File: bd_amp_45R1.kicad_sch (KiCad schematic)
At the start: 53 parts, among them Q2101 2SC3357, Q2102 2SC3357, T2101 XFMR_RF_BIFILAR, T2102 XFMR_RF_BIFILAR, U2101 AS169-73, U2102 AS169-73

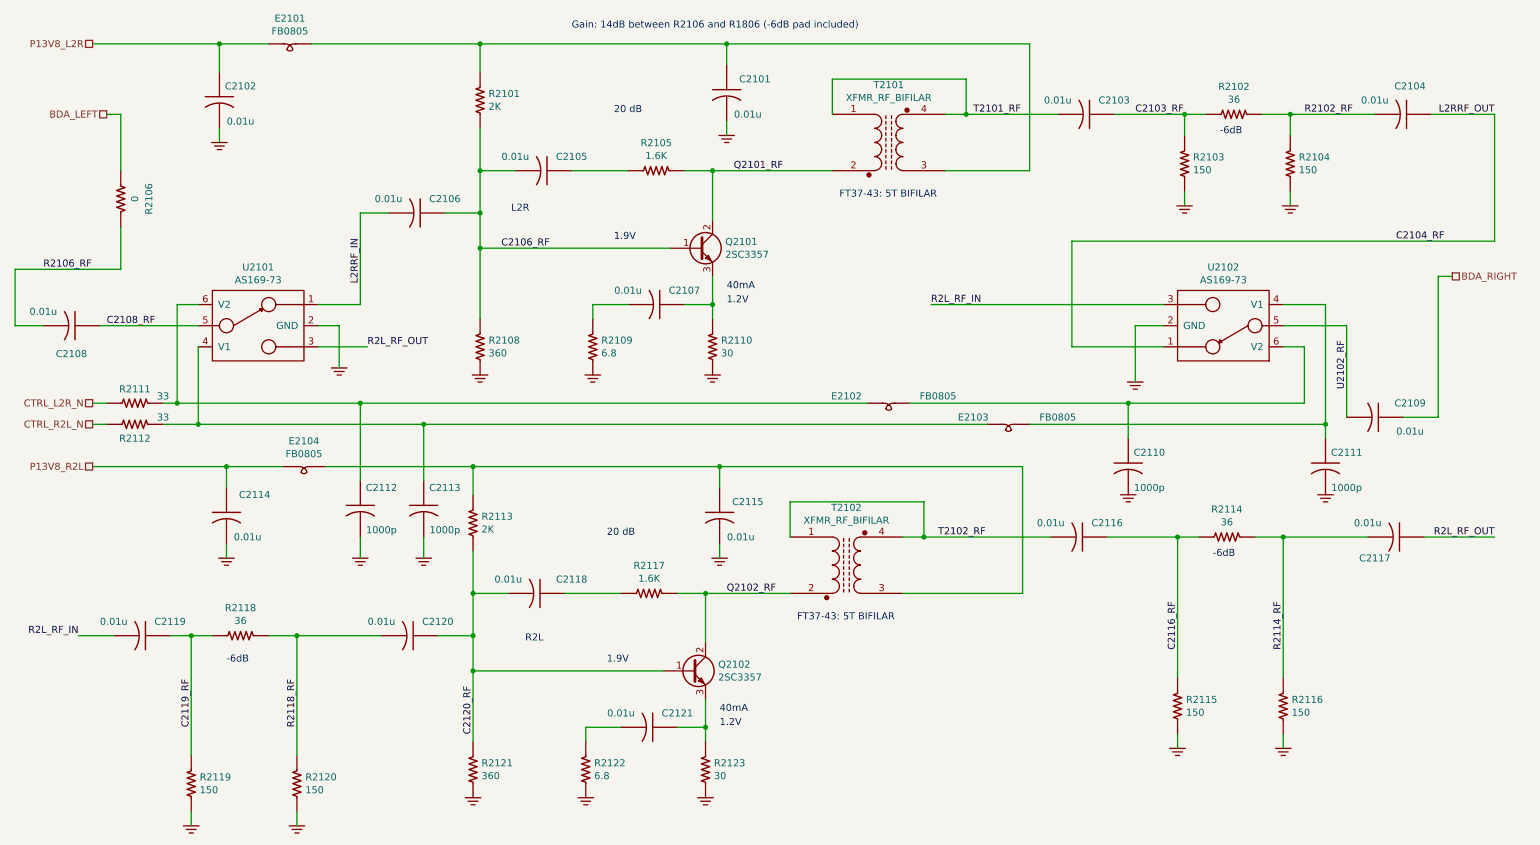
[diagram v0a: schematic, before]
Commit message: Update pcb database to version 6
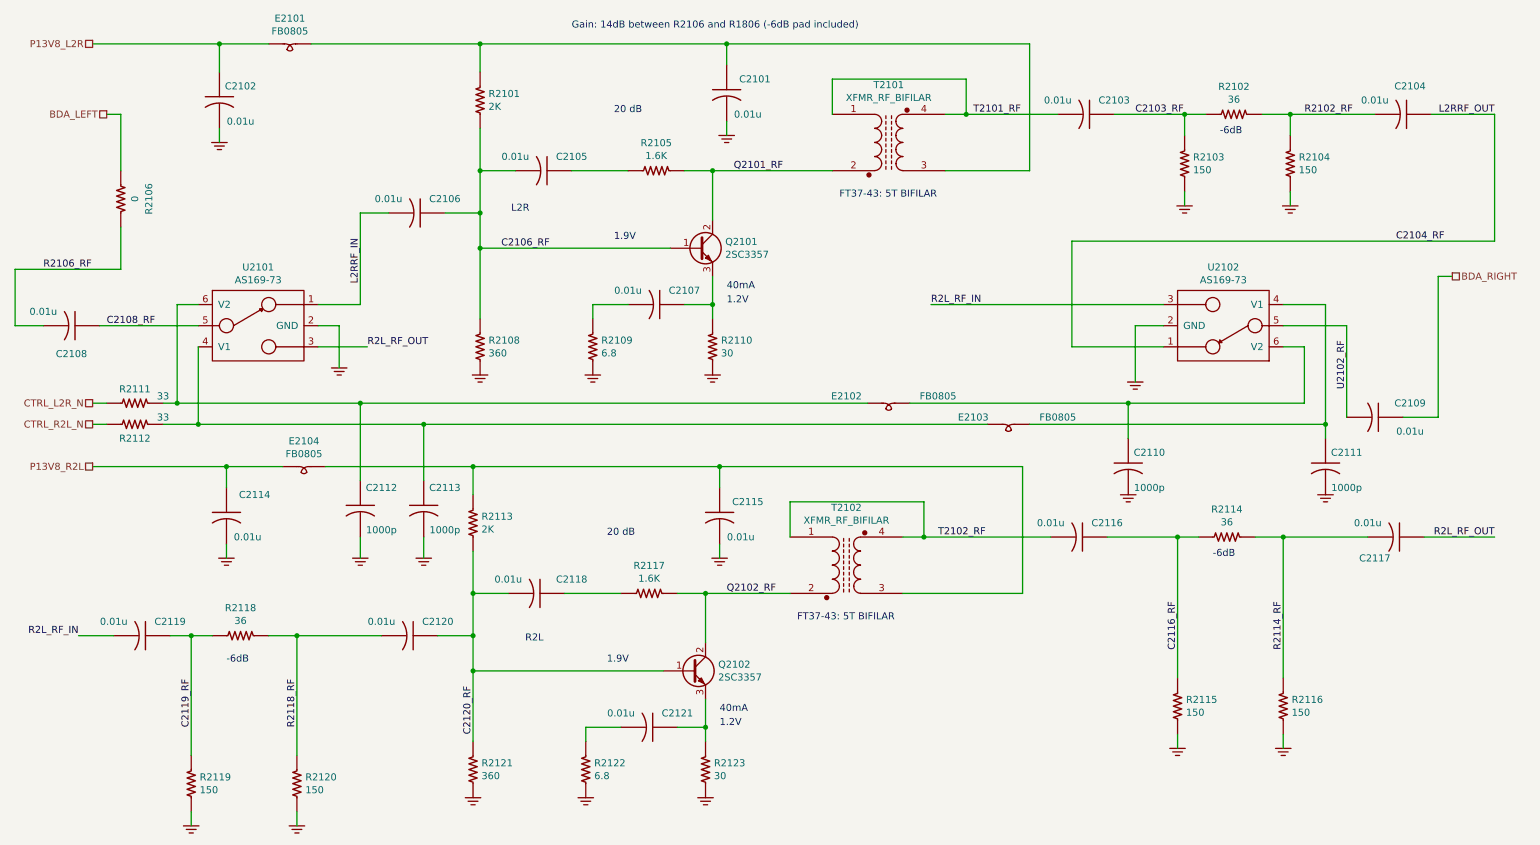
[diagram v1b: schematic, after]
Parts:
- C2101, C2102, C2103, C2104, C2105, C2106, C2107, C2108, C2109, C2114, C2115, C2116, C2117, C2118, C2119, C2120, C2121: footprint Capacitor_SMD:C_0805_2012Metric_Pad1.15x1.40mm_HandSolder -> Capacitor_SMD:C_0603_1608Metric; symbol Custom:C_US -> custom:C_US; PartNumber 800238-103 -> 800063-XXX
- C2110, C2111, C2112, C2113: footprint Capacitor_SMD:C_0805_2012Metric_Pad1.15x1.40mm_HandSolder -> Capacitor_SMD:C_0603_1608Metric; symbol Custom:C_US -> custom:C_US; PartNumber 800238-102 -> 800063-XXX
- E2101, E2102, E2103, E2104: footprint Inductor_SMD:L_0805_2012Metric_Pad1.15x1.40mm_HandSolder -> Inductor_SMD:L_0805_2012Metric; symbol Custom:FB0805 -> custom:FB0805; PartNumber 800245-601 -> 80000X-XXX
- Q2101, Q2102: symbol Custom:2SC3357 -> custom:2SC3357
- R2101, R2113: symbol Custom:R_US -> custom:R_US; PartNumber 800235-202 -> 800XXX-XXX
- R2102, R2114, R2118: symbol Custom:R_US -> custom:R_US; PartNumber 800235-360 -> 800XXX-XXX
- R2103, R2104, R2115, R2116, R2119, R2120: symbol Custom:R_US -> custom:R_US; PartNumber 800235-151 -> 800XXX-XXX
- R2105, R2117: symbol Custom:R_US -> custom:R_US; PartNumber 800235-162 -> 800XXX-XXX
- R2106: symbol Custom:R_US -> custom:R_US; PartNumber 800235-000 -> 800XXX-XXX
- R2108, R2121: symbol Custom:R_US -> custom:R_US; PartNumber 800235-361 -> 800XXX-XXX
- R2109, R2122: symbol Custom:R_US -> custom:R_US; PartNumber 800235-068 -> 800XXX-XXX
- R2110, R2123: symbol Custom:R_US -> custom:R_US; PartNumber 800235-300 -> 800XXX-XXX
- R2111, R2112: symbol Custom:R_US -> custom:R_US; PartNumber 800235-330 -> 800XXX-XXX
- T2101, T2102: symbol Custom:XFMR_RF_BIFILAR -> custom:XFMR_RF_BIFILAR
- U2101, U2102: footprint Package_TO_SOT_SMD:SOT-23-6_Handsoldering -> Package_TO_SOT_SMD:SOT-23-6; symbol Custom:AS169-73 -> custom:AS169-73

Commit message: Fix BOM part number errors and out of sync footprints which happened during conversion from Kicad 5 to 6
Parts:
- C2101, C2102, C2103, C2104, C2105, C2106, C2107, C2108, C2109, C2114, C2115, C2116, C2117, C2118, C2119, C2120, C2121: footprint Capacitor_SMD:C_0603_1608Metric -> Capacitor_SMD:C_0805_2012Metric_Pad1.18x1.45mm_HandSolder; PartNumber 800063-XXX -> 800238-103
- C2110, C2111, C2112, C2113: footprint Capacitor_SMD:C_0603_1608Metric -> Capacitor_SMD:C_0805_2012Metric_Pad1.18x1.45mm_HandSolder; PartNumber 800063-XXX -> 800239-102
- E2101, E2102, E2103, E2104: PartNumber 80000X-XXX -> 800245-601
- R2101, R2113: PartNumber 800XXX-XXX -> 800235-202
- R2102, R2114, R2118: PartNumber 800XXX-XXX -> 800235-360
- R2103, R2104, R2115, R2116, R2119, R2120: PartNumber 800XXX-XXX -> 800235-151
- R2105, R2117: PartNumber 800XXX-XXX -> 800235-162
- R2106: PartNumber 800XXX-XXX -> 800235-000
- R2108, R2121: PartNumber 800XXX-XXX -> 800235-361
- R2109, R2122: PartNumber 800XXX-XXX -> 800235-068
- R2110, R2123: PartNumber 800XXX-XXX -> 800235-300
- R2111, R2112: PartNumber 800XXX-XXX -> 800235-330

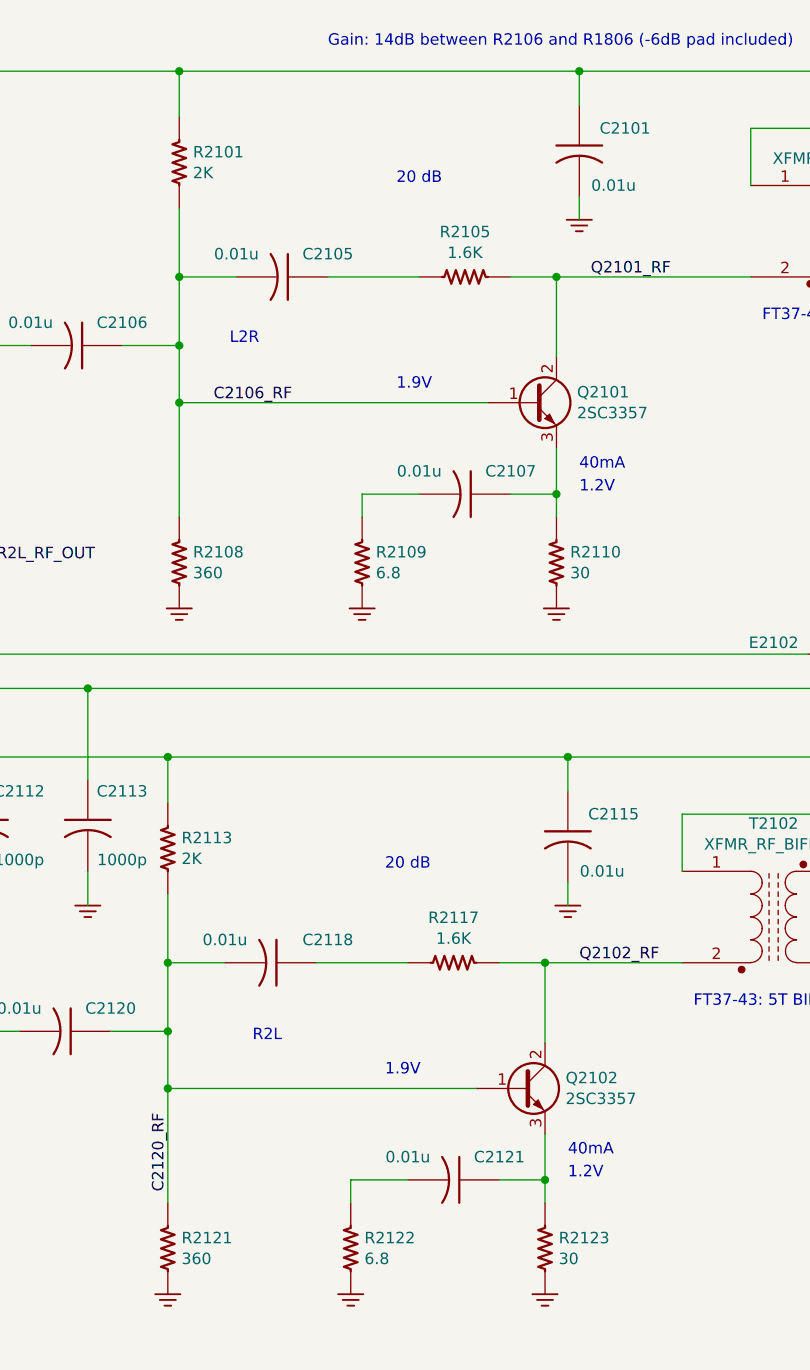
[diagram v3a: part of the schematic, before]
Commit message: Change bias resistors on 2SC3357 amplifiers to stay under 12V across Vbe.
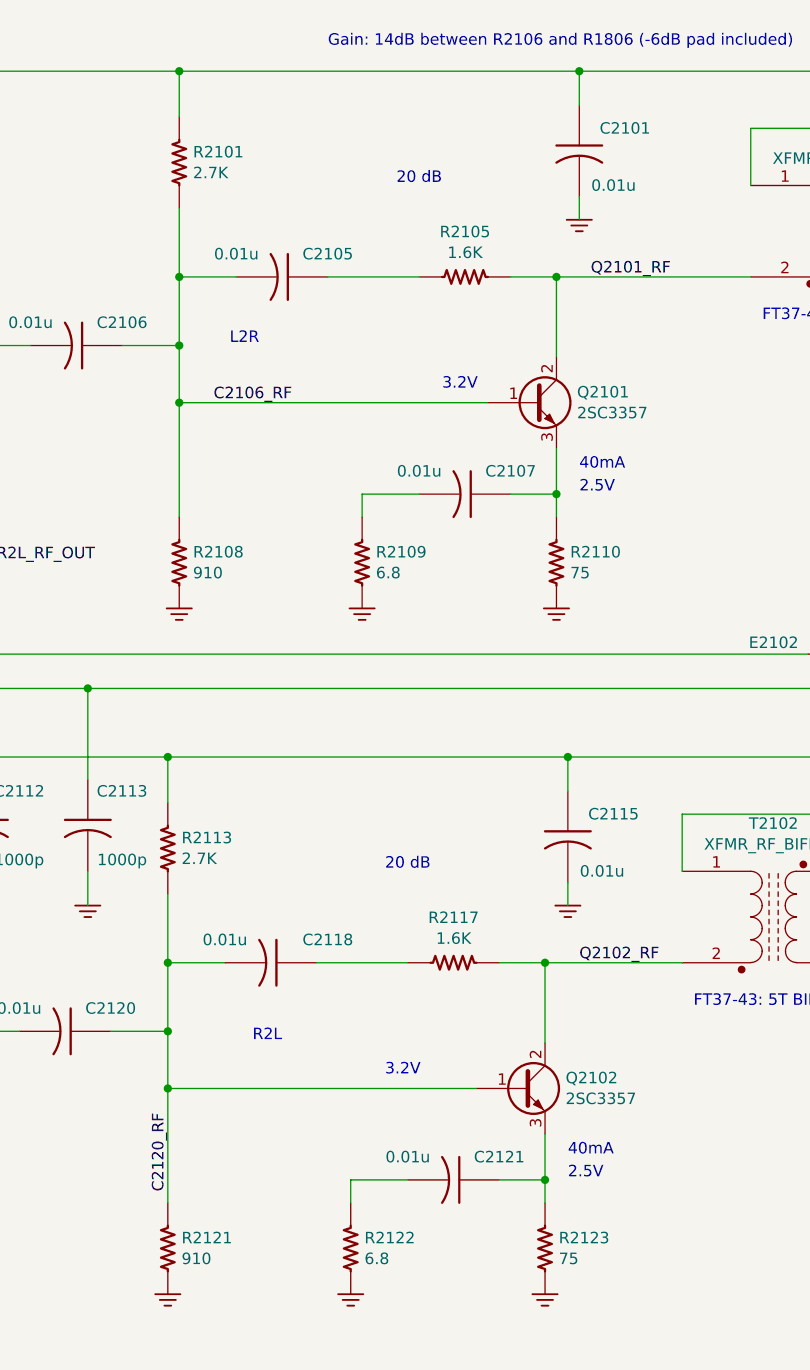
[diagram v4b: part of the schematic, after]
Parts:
- R2101, R2113: value 2K -> 2.7K; PartNumber 800235-202 -> 800235-272
- R2108, R2121: value 360 -> 910; PartNumber 800235-361 -> 800235-911
- R2110, R2123: value 30 -> 75; PartNumber 800235-300 -> 800235-750
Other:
- note added: "2.5V"
- note added: "3.2V"
- note removed: "1.2V"
- note removed: "1.9V"
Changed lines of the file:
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@@
-    (effects (font (size 1.27 1.27)) (justify left bottom))
-  )
-  (text "1.9V\n" (at 120.65 55.88 0)
     (effects (font (size 1.27 1.27)) (justify left bottom))
   )
@@
     (effects (font (size 1.27 1.27)) (justify left bottom))
   )
-  (text "1.9V\n" (at 119.38 132.08 0)
-    (effects (font (size 1.27 1.27)) (justify left bottom))
-  )
-  (text "1.2V" (at 139.7 143.51 0)
+  (text "2.5V" (at 140.97 67.31 0)
+    (effects (font (size 1.27 1.27)) (justify left bottom))
+  )
+  (text "3.2V\n" (at 119.38 132.08 0)
+    (effects (font (size 1.27 1.27)) (justify left bottom))
+  )
+  (text "2.5V\n" (at 139.7 143.51 0)
     (effects (font (size 1.27 1.27)) (justify left bottom))
   )
@@
     (effects (font (size 1.27 1.27)) (justify right bottom))
   )
+  (text "3.2V" (at 125.73 55.88 0)
+    (effects (font (size 1.27 1.27)) (justify left bottom))
+  )
   (text "FT37-43: 5T BIFILAR" (at 153.67 124.46 0)
     (effects (font (size 1.27 1.27)) (justify left bottom))
@@
   )
   (text "40mA" (at 140.97 64.77 0)
-    (effects (font (size 1.27 1.27)) (justify left bottom))
-  )
-  (text "1.2V" (at 140.97 67.31 0)
     (effects (font (size 1.27 1.27)) (justify left bottom))
   )
@@
       (effects (font (size 1.27 1.27)) (justify left))
     )
-    (property "Value" "30" (id 1) (at 139.954 76.073 0)
+    (property "Value" "75" (id 1) (at 139.954 76.073 0)
       (effects (font (size 1.27 1.27)) (justify left))
     )
@@
       (effects (font (size 1.524 1.524)))
     )
-    (property "PartNumber" "800235-300" (id 4) (at 143.002 72.39 90)
+    (property "PartNumber" "800235-750" (id 4) (at 143.002 72.39 90)
       (effects (font (size 1.524 1.524)) hide)
     )
@@
       (effects (font (size 1.27 1.27)) (justify left))
     )
-    (property "Value" "2K" (id 1) (at 98.044 31.623 0)
+    (property "Value" "2.7K" (id 1) (at 98.044 31.623 0)
       (effects (font (size 1.27 1.27)) (justify left))
     )
@@
       (effects (font (size 1.524 1.524)))
     )
-    (property "PartNumber" "800235-202" (id 4) (at 101.092 27.94 90)
+    (property "PartNumber" "800235-272" (id 4) (at 101.092 27.94 90)
       (effects (font (size 1.524 1.524)) hide)
     )
@@
       (effects (font (size 1.27 1.27)) (justify left))
     )
-    (property "Value" "30" (id 1) (at 138.684 152.273 0)
+    (property "Value" "75" (id 1) (at 138.684 152.273 0)
       (effects (font (size 1.27 1.27)) (justify left))
     )
@@
       (effects (font (size 1.524 1.524)))
     )
-    (property "PartNumber" "800235-300" (id 4) (at 141.732 148.59 90)
+    (property "PartNumber" "800235-750" (id 4) (at 141.732 148.59 90)
       (effects (font (size 1.524 1.524)) hide)
     )
@@
       (effects (font (size 1.27 1.27)) (justify left))
     )
-    (property "Value" "2K" (id 1) (at 96.774 107.823 0)
+    (property "Value" "2.7K" (id 1) (at 96.774 107.823 0)
       (effects (font (size 1.27 1.27)) (justify left))
     )
@@
       (effects (font (size 1.524 1.524)))
     )
-    (property "PartNumber" "800235-202" (id 4) (at 99.822 104.14 90)
+    (property "PartNumber" "800235-272" (id 4) (at 99.822 104.14 90)
       (effects (font (size 1.524 1.524)) hide)
     )
@@
       (effects (font (size 1.27 1.27)) (justify left))
     )
-    (property "Value" "360" (id 1) (at 98.044 76.073 0)
+    (property "Value" "910" (id 1) (at 98.044 76.073 0)
       (effects (font (size 1.27 1.27)) (justify left))
     )
@@
       (effects (font (size 1.524 1.524)))
     )
-    (property "PartNumber" "800235-361" (id 4) (at 101.092 72.39 90)
+    (property "PartNumber" "800235-911" (id 4) (at 101.092 72.39 90)
       (effects (font (size 1.524 1.524)) hide)
     )
@@
       (effects (font (size 1.27 1.27)) (justify left))
     )
-    (property "Value" "360" (id 1) (at 96.774 152.273 0)
+    (property "Value" "910" (id 1) (at 96.774 152.273 0)
       (effects (font (size 1.27 1.27)) (justify left))
     )
@@
       (effects (font (size 1.524 1.524)))
     )
-    (property "PartNumber" "800235-361" (id 4) (at 99.822 148.59 90)
-      (effects (font (size 1.524 1.524)) hide)
-    )
+    (property "PartNumber" "800235-911" (id 4) (at 99.822 148.59 90)
+      (effects (font (size 1.524 1.524)) hide)
+    )
